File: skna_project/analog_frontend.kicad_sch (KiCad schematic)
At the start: 26 parts, among them J6 ECG+, J7 ECG-, J8 RL, U5 INA333xxDGK, U6 OPA333xxD, U7 OPA333xxD, U8 OPA333xxD

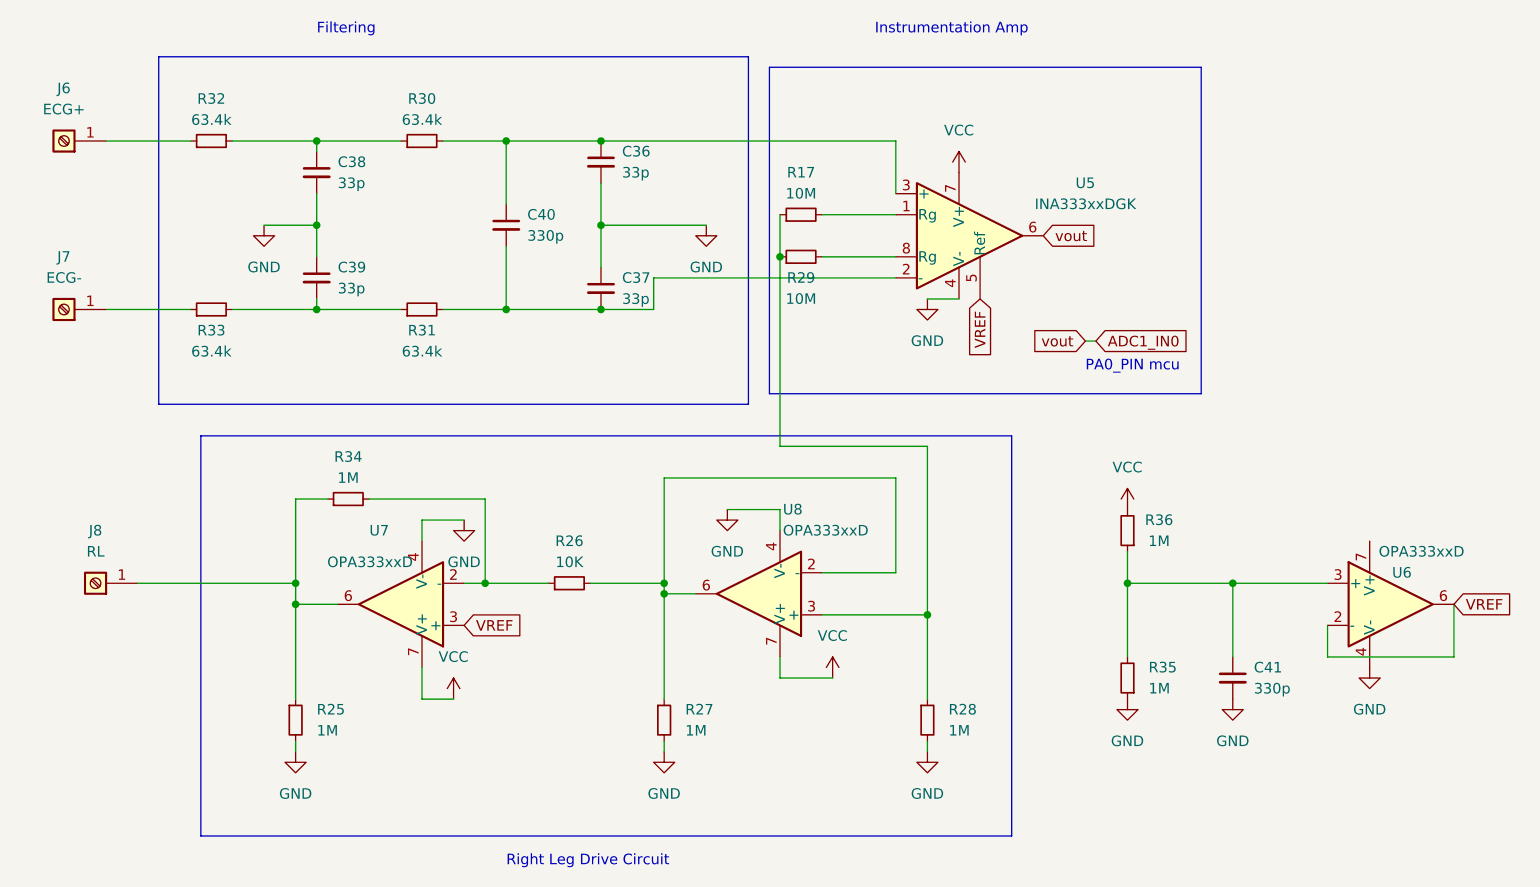
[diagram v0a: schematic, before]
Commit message: Replaced ADS129 with ADS8232
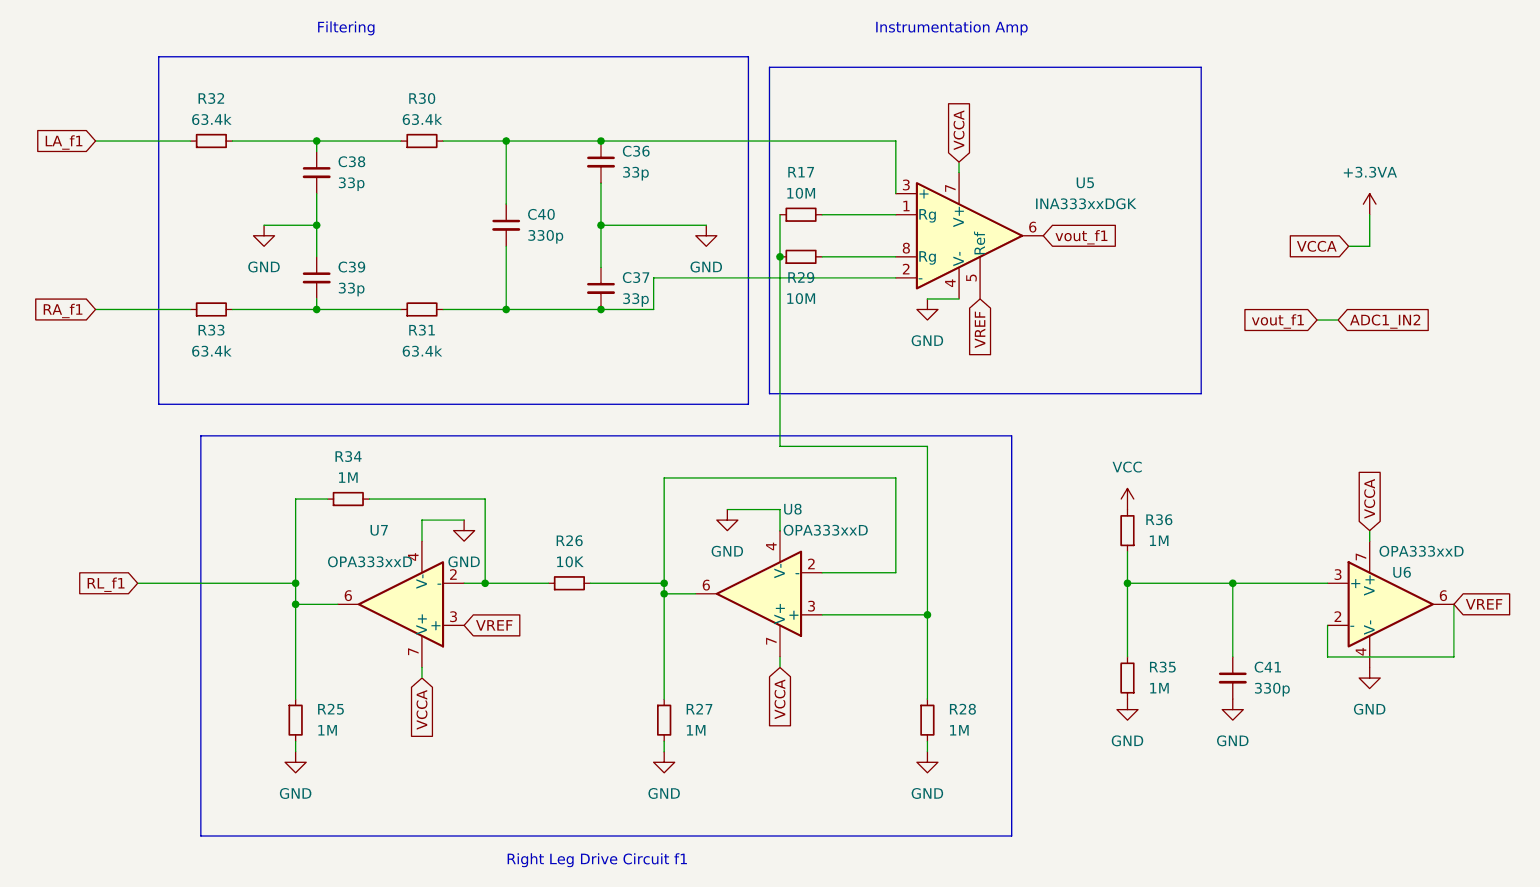
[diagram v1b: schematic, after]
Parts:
- removed J6: ECG+, symbol Connector:Screw_Terminal_01x01
- removed J7: ECG-, symbol Connector:Screw_Terminal_01x01
- removed J8: RL, symbol Connector:Screw_Terminal_01x01
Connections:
- net VCC: no longer U5.7 (V+), U7.7 (V+), U8.7 (V+)
- net RL_f1: now reaches R25.1, R34.1, U7.6
- net RA_f1: now reaches R33.1
- net LA_f1: now reaches R32.1
- net +3.3VA: now reaches U6.7 (V+)
- net +3.3VA: now also U5.7 (V+), U7.7 (V+), U8.7 (V+)
- net ADC1_IN0 renamed ADC1_IN2
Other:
- note added: "Right Leg Drive Circuit f1"
- note removed: "PA0_PIN mcu"
- note removed: "Right Leg Drive Circuit"
